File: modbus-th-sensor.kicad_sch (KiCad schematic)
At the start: 38 parts, among them J1 Screw Terminal, J2 FTDI Serial, J3 ICSP, J4 Sensor Board, J5 I2C, U1 ATmega328P-A, U3 THVD2410DR, U5 AP63203WU, Y1 8MHz

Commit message: Finished routing main board
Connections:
- net RXEN: now also U1.1 (PD3); no longer U1.32 (PD2)
- net TXEN: now also U1.32 (PD2); no longer U1.1 (PD3)
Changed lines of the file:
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@@
 		)
 	)
+	(label "VIN_PROT"
+		(at 106.68 31.75 0)
+		(effects
+			(font
+				(size 1.27 1.27)
+			)
+			(justify left bottom)
+		)
+	)
+	(label "VIN_FUSED"
+		(at 88.9 31.75 0)
+		(effects
+			(font
+				(size 1.27 1.27)
+			)
+			(justify left bottom)
+		)
+	)
 	(global_label "TXO"
 		(shape input)
@@
 		)
 	)
-	(global_label "TXEN"
+	(global_label "RXEN"
 		(shape input)
 		(at 121.92 148.59 0)
@@
 		)
 		(property "Intersheetrefs" "${INTERSHEET_REFS}"
-			(at 127.937 148.59 0)
+			(at 128.1751 148.59 0)
 			(hide yes)
 			(show_name no)
@@
 		)
 	)
-	(global_label "RXEN"
+	(global_label "TXEN"
 		(shape input)
 		(at 121.92 146.05 0)
@@
 		)
 		(property "Intersheetrefs" "${INTERSHEET_REFS}"
-			(at 128.1751 146.05 0)
+			(at 127.937 146.05 0)
 			(hide yes)
 			(show_name no)
@@
 		)
 	)
-	(label "VIN_FUSED"
-		(at 88.9 31.75 0)
-		(effects
-			(font
-				(size 1.27 1.27)
-			)
-			(justify left bottom)
-		)
-	)
-	(label "VIN_PROT"
-		(at 106.68 31.75 0)
-		(effects
-			(font
-				(size 1.27 1.27)
-			)
-			(justify left bottom)
-		)
-	)

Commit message: Main board tidy ups - Move U5 FB track away from SW node, BST pad and L1 - Add extra GND vias - Move R1 (RESET pull-up) next to U1 - Include J5 in the BOM, consistent with other hand-fitted connectors
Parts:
- J5: now in the parts list
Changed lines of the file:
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@@
 		(body_style 1)
 		(exclude_from_sim no)
-		(in_bom no)
+		(in_bom yes)
 		(on_board yes)
 		(in_pos_files no)

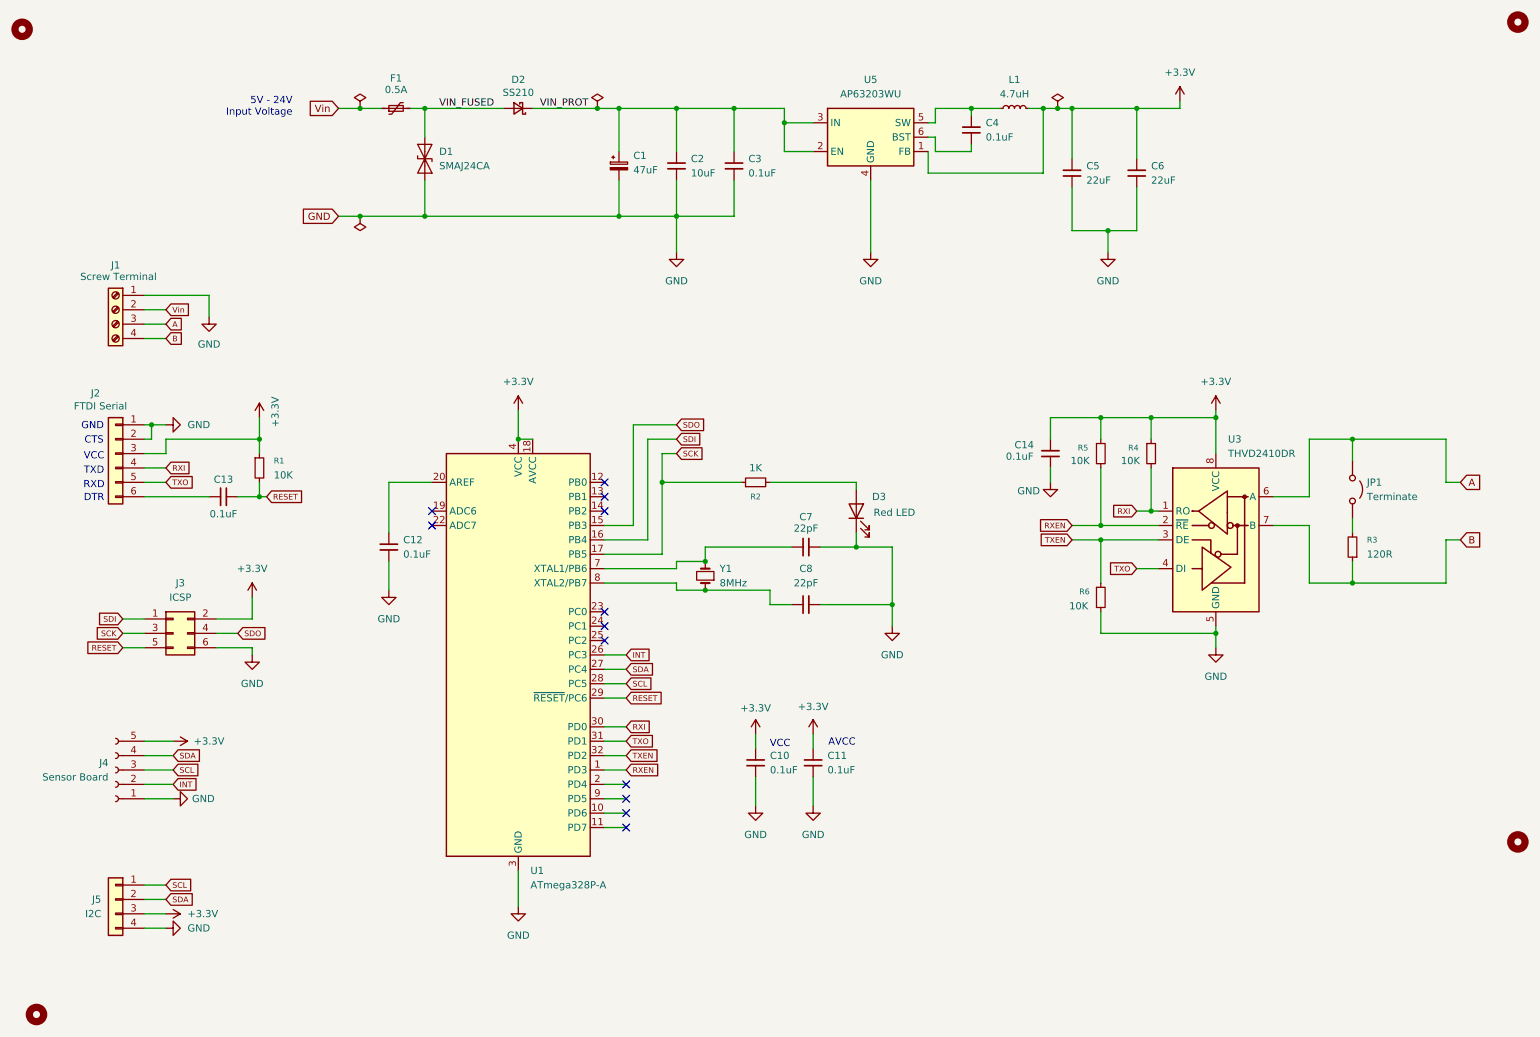
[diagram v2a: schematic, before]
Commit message: Re-worked main board for the Camdenboss CBRS01 series of enclosures - New 73.32 x 73.32 mm outline, with M2.5 mounting holes - Moved the sensor notch so the breakout's mounting hole sits on the lid's centre post - Added back the Unit ID jumper header
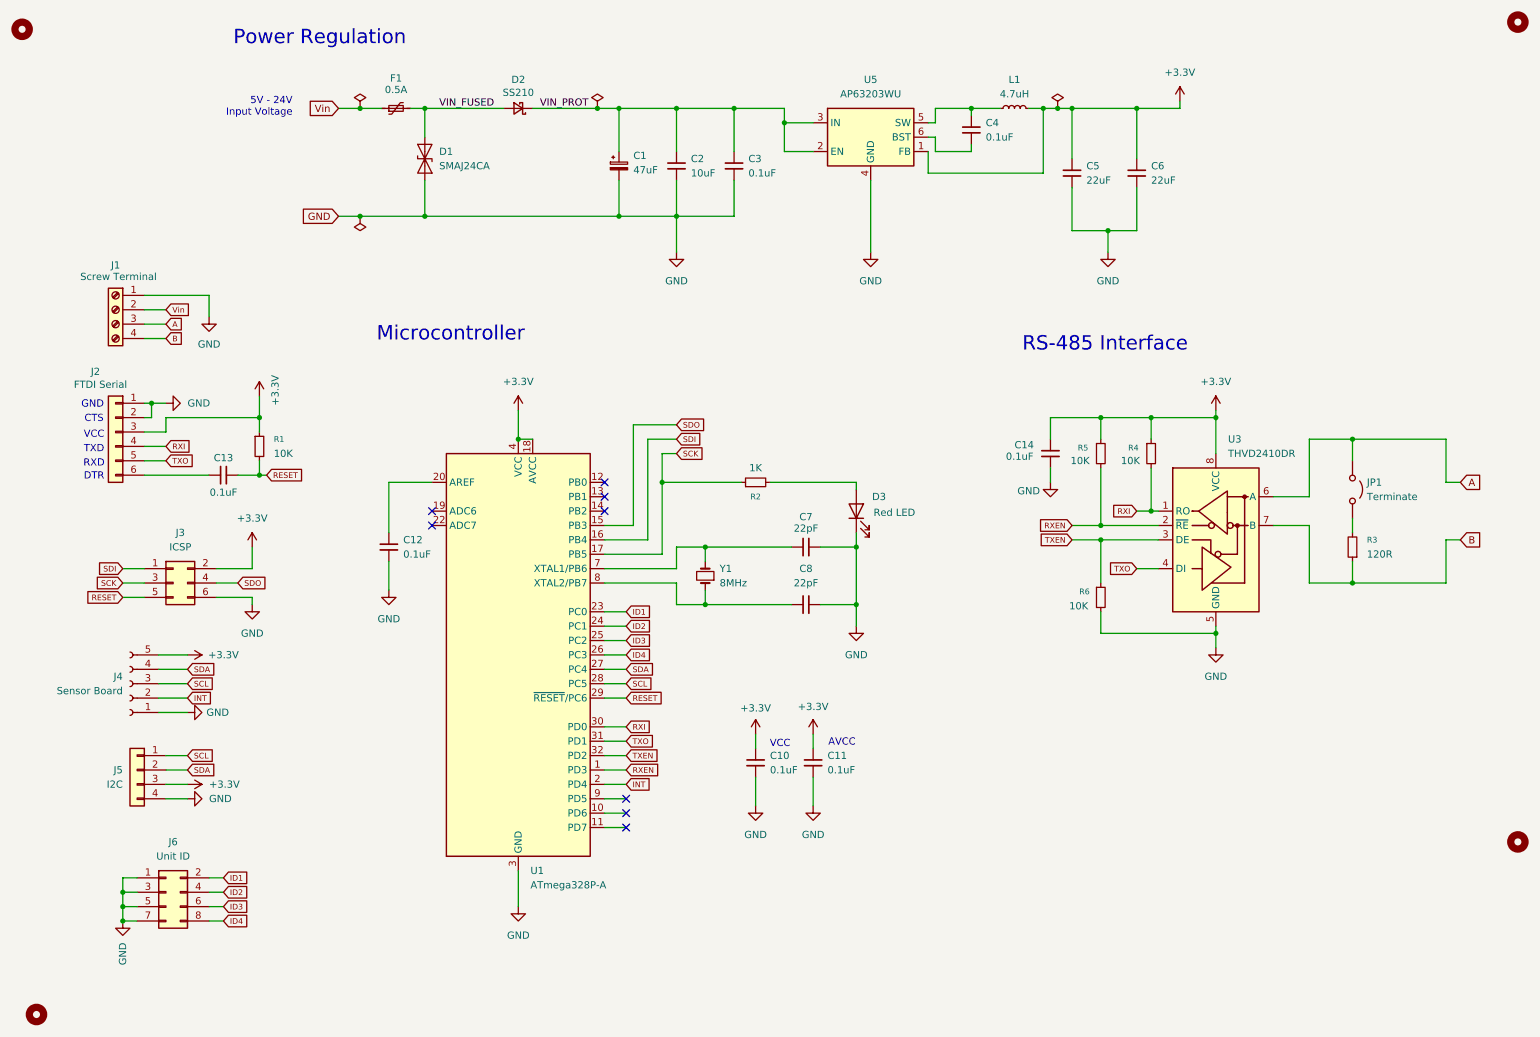
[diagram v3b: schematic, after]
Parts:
- added J6: Unit ID, Connector_PinHeader_2.54mm:PinHeader_2x04_P2.54mm_Vertical, symbol Connector_Generic:Conn_02x04_Odd_Even
- H1, H2, H3, H4: footprint MountingHole:MountingHole_3.2mm_M3 -> MountingHole:MountingHole_2.7mm_M2.5
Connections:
- net GND: now also J6.1 (Pin_1), J6.3 (Pin_3), J6.5 (Pin_5), J6.7 (Pin_7)
- net INT: now also U1.2 (PD4); no longer U1.26 (PC3)
- net ID1: now reaches U1.23 (PC0)
- net ID1: now also J6.2 (Pin_2)
- net ID2: now reaches U1.24 (PC1)
- net ID2: now also J6.4 (Pin_4)
- net ID3: now reaches U1.25 (PC2)
- net ID3: now also J6.6 (Pin_6)
- new net ID4: J6.8 (Pin_8), U1.26 (PC3)
- no-connect marks 12 -> 8
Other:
- note added: "Microcontroller"
- note added: "Power Regulation"
- note added: "RS-485 Interface"
- moved on the sheet: C13, J2, J3, J4, J5, R1

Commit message: Moved buck converter FB back to the front layer Minor value and label changes.
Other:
- title: (none) -> Modbus Room Sensor
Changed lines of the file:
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@@
 	(generator_version "10.0")
 	(paper "A4")
+	(title_block
+		(title "Modbus Room Sensor")
+		(date "2026-10-21")
+		(rev "2")
+	)
 	(text "AVCC"
 		(exclude_from_sim no)
